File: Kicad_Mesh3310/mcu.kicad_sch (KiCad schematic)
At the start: 43 parts, among them U13 NRF52840-QIAA-R, U4 MX25R1635FZNIH0, U7 USBLC6-2P6, X2 S201632M10PF10PPM 32MHz, X4 32.768KHz

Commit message: Schema afgemaakt, 6-laags layout, LCSC-onderdelen en productiebestanden
- schema opgeschoond en aangevuld (ERC 0)
- bord naar 6 lagen (JLC06161H-3313), volledig gerouteerd, DRC 0
- LTE via U.FL, USB via bodemconnector J4
- LCSC-nummers voor alle onderdelen, datasheets toegevoegd
- gerbers, boorbestanden, positiebestand en stuklijst in productie/
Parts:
- ANT2: LCSC (none) -> C17605137
- C1: footprint Resistor_SMD:R_0201_0603Metric -> Capacitor_SMD:C_0201_0603Metric; LCSC C1525 -> C408130
- C22, C29: value 18pF -> 15pF; LCSC C32949 -> C5142550
- C30: LCSC C1544 -> C301906
- C31, C32: LCSC C15195 -> C50391
- C34, C41, C58: LCSC C1525 -> C408130
- C35, C37, C39, C40, C47, C50: footprint Capacitor_SMD:C_0201_0603Metric -> Capacitor_SMD:C_0402_1005Metric; LCSC C12530 -> C107370
- C36: footprint Capacitor_SMD:C_0201_0603Metric -> Capacitor_SMD:C_0402_1005Metric; LCSC C5199872 -> C52923
- C38: LCSC C82219 -> C301920
- C45: LCSC C1546 -> C62550
- C46: LCSC C1543 -> C18164584
- L1: LCSC C86065 -> C42144
- L4: LCSC C86065 -> C54929554
- L5: footprint Inductor_SMD:L_0201_0603Metric -> Inductor_SMD:L_0603_1608Metric
- L6: LCSC C381880 -> C52109780
- R3, R57, R58: LCSC C17168 -> C473473
- U4: LCSC (none) -> C6930062
- X4: LCSC C95361 -> C97605
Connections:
- net GND: now also U4.9 (EXP)
- no-connect marks 4 -> 2
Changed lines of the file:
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@@
 	)
 	(no_connect
-		(at 233.68 97.79)
-	)
-	(no_connect
 		(at 101.6 100.33)
 	)
@@
 		(at 101.6 57.15)
 	)
-	(no_connect
-		(at 115.57 118.11)
-	)
 	(wire
 		(pts
@@
 			)
 		)
-		(property "Footprint" "Capacitor_SMD:C_0201_0603Metric"
+		(property "Footprint" "Capacitor_SMD:C_0402_1005Metric"
 			(at 147.32 38.1 0)
 			(effects
@@
 			)
 		)
-		(property "LCSC" "C12530"
+		(property "LCSC" "C107370"
 			(at 147.32 38.1 0)
 			(effects
@@
 			)
 		)
-		(property "LCSC" "C1544"
+		(property "LCSC" "C301906"
 			(at 242.57 144.78 0)
 			(effects
@@
 			)
 		)
-		(property "Footprint" "Capacitor_SMD:C_0201_0603Metric"
+		(property "Footprint" "Capacitor_SMD:C_0402_1005Metric"
 			(at 125.73 38.1 0)
 			(effects
@@
 			)
 		)
-		(property "LCSC" "C12530"
+		(property "LCSC" "C107370"
 			(at 125.73 38.1 0)
 			(effects
@@
 			)
 		)
-		(property "LCSC" "C15195"
+		(property "LCSC" "C50391"
 			(at 247.65 26.67 90)
 			(effects
@@
 			)
 		)
-		(property "Footprint" "Capacitor_SMD:C_0201_0603Metric"
+		(property "Footprint" "Capacitor_SMD:C_0402_1005Metric"
 			(at 177.8 54.61 0)
 			(effects
@@
 			)
 		)
-		(property "LCSC" "C12530"
+		(property "LCSC" "C107370"
 			(at 177.8 54.61 0)
 			(effects
@@
 			)
 		)
+		(property "LCSC" "C17605137"
+			(at 218.44 234.62 0)
+			(effects
+				(font
+					(size 1.27 1.27)
+				)
+				(justify left top)
+				(hide yes)
+			)
+		)
 		(property "Datasheet" "https://www.johansontechnology.com/docs/1996/2450AT42E0100_6fzbZoe.pdf"
 			(at 218.44 334.62 0)
@@
 			)
 		)
+		(property "LCSC" "C6930062"
+			(at 73.66 175.26 0)
+			(effects
+				(font
+					(size 1.27 1.27)
+				)
+				(justify bottom)
+				(hide yes)
+			)
+		)
 		(property "Datasheet" ""
 			(at 73.66 175.26 0)
@@
 			)
 		)
-		(property "Footprint" "Capacitor_SMD:C_0201_0603Metric"
+		(property "Footprint" "Capacitor_SMD:C_0402_1005Metric"
 			(at 137.16 38.1 0)
 			(effects
@@
 			)
 		)
-		(property "LCSC" "C12530"
+		(property "LCSC" "C107370"
 			(at 137.16 38.1 0)
 			(effects
@@
 			)
 		)
-		(property "LCSC" "C86065"
+		(property "LCSC" "C54929554"
 			(at 236.22 139.7 90)
 			(effects
@@
 			)
 		)
-		(property "LCSC" "C95361"
+		(property "LCSC" "C97605"
 			(at 255.27 33.02 0)
 			(effects
@@
 			)
 		)
-		(property "LCSC" "C17168"
+		(property "LCSC" "C473473"
 			(at 120.65 140.97 90)
 			(effects
@@
 			)
 		)
-		(property "LCSC" "C17168"
+		(property "LCSC" "C473473"
 			(at 265.43 139.7 90)
 			(effects
@@
 			)
 		)
-		(property "LCSC" "C1546"
+		(property "LCSC" "C62550"
 			(at 158.75 67.31 90)
 			(effects
@@
 			)
 		)
-		(property "Footprint" "Inductor_SMD:L_0201_0603Metric"
+		(property "Footprint" "Inductor_SMD:L_0603_1608Metric"
 			(at 118.11 54.61 0)
 			(effects
@@
 			)
 		)
-		(property "Value" "18pF"
+		(property "Value" "15pF"
 			(at 209.804 27.94 90)
 			(effects
@@
 			)
 		)
-		(property "LCSC" "C32949"
+		(property "LCSC" "C5142550"
 			(at 208.28 26.67 0)
 			(effects
@@
 			)
 		)
-		(property "LCSC" "C82219"
+		(property "LCSC" "C301920"
 			(at 134.62 81.28 90)
 			(effects
@@
 			)
 		)
-		(property "LCSC" "C15195"
+		(property "LCSC" "C50391"
 			(at 247.65 39.37 90)
 			(effects
@@
 			)
 		)
-		(property "LCSC" "C381880"
+		(property "LCSC" "C52109780"
 			(at 128.27 54.61 90)
 			(effects
@@
 			)
 		)
-		(property "Value" "18pF"
+		(property "Value" "15pF"
 			(at 209.804 40.64 90)
 			(effects
@@
 			)
 		)
-		(property "LCSC" "C32949"
+		(property "LCSC" "C5142550"
 			(at 208.28 39.37 0)
 			(effects
@@
 			)
 		)
-		(property "LCSC" "C17168"
+		(property "LCSC" "C473473"
 			(at 120.65 143.51 90)
 			(effects
@@
 			)
 		)
-		(property "LCSC" "C1543"
+		(property "LCSC" "C18164584"
 			(at 158.75 72.39 90)
 			(effects
@@
 			)
 		)
-		(property "LCSC" "C1525"
+		(property "LCSC" "C408130"
 			(at 118.11 180.34 90)
 			(effects
@@
 			)
 		)
-		(property "LCSC" "C86065"
+		(property "LCSC" "C42144"
 			(at 246.38 144.78 90)
 			(effects
@@
 			)
 		)
-		(property "LCSC" "C1525"
+		(property "LCSC" "C408130"
 			(at 158.75 62.23 90)
 			(effects
@@
 			)
 		)
-		(property "Footprint" "Capacitor_SMD:C_0201_0603Metric"
+		(property "Footprint" "Capacitor_SMD:C_0402_1005Metric"
 			(at 123.4948 77.47 0)
 			(effects
@@
 			)
 		)
-		(property "LCSC" "C5199872"
+		(property "LCSC" "C52923"
 			(at 124.46 81.28 0)
 			(effects
@@
 			)
 		)
-		(property "LCSC" "C1525"
+		(property "LCSC" "C408130"
 			(at 157.48 38.1 90)
 			(effects
@@
 			)
 		)
-		(property "Footprint" "Capacitor_SMD:C_0201_0603Metric"
+		(property "Footprint" "Capacitor_SMD:C_0402_1005Metric"
 			(at 111.76 38.1 0)
 			(effects
@@
 			)
 		)
-		(property "LCSC" "C12530"
+		(property "LCSC" "C107370"
 			(at 111.76 38.1 0)
 			(effects
@@
 			)
 		)
-		(property "Footprint" "Capacitor_SMD:C_0201_0603Metric"
+		(property "Footprint" "Capacitor_SMD:C_0402_1005Metric"
 			(at 167.64 59.69 0)
 			(effects
@@
 			)
 		)
-		(property "LCSC" "C12530"
+		(property "LCSC" "C107370"
 			(at 167.64 59.69 0)
 			(effects
@@
 			)
 		)
-		(property "Footprint" "Resistor_SMD:R_0201_0603Metric"
+		(property "Footprint" "Capacitor_SMD:C_0201_0603Metric"
 			(at 25.4 85.09 0)
 			(effects
@@
 			)
 		)
-		(property "LCSC" "C1525"
+		(property "LCSC" "C408130"
 			(at 25.4 85.09 90)
 			(effects
@@
 		)
 	)
+	(wire
+		(pts
+			(xy 96.52 182.88) (xy 96.52 187.96)
+		)
+		(stroke
+			(width 0)
+			(type default)
+		)
+	)

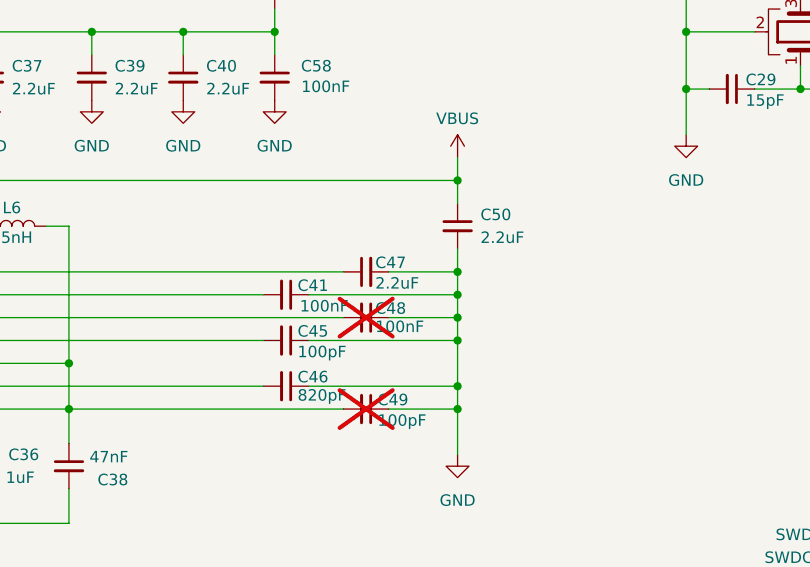
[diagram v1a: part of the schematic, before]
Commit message: Rev. F + G: controleronde, TPS3420 aan/uit-knop, FLASH_CS pull-up, RF4 DNP, U.FL-variant LoRa
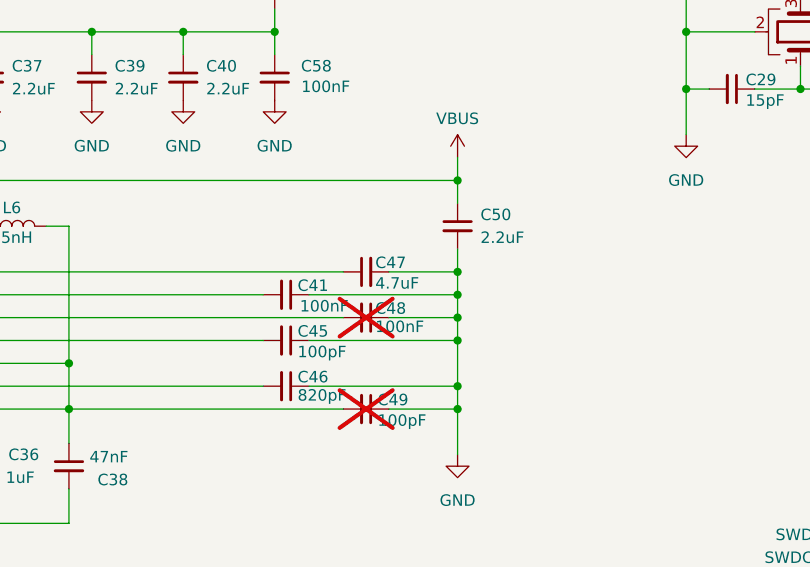
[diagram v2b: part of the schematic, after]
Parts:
- C47: value 2.2uF -> 4.7uF; LCSC C107370 -> C23733
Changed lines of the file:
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@@
 		(title "Mainboard replacement for Nokia 3310")
 		(date "29-12-2025")
-		(rev "Rev A")
+		(rev "Rev G")
 		(company "Mesh3310")
 		(comment 1 "JDJ electronics")
@@
 			)
 		)
-		(property "Value" "2.2uF"
+		(property "Value" "4.7uF"
 			(at 168.656 60.96 90)
 			(effects
@@
 			)
 		)
-		(property "LCSC" "C107370"
+		(property "LCSC" "C23733"
 			(at 167.64 59.69 0)
 			(effects
